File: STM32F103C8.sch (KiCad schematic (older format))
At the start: 25 parts

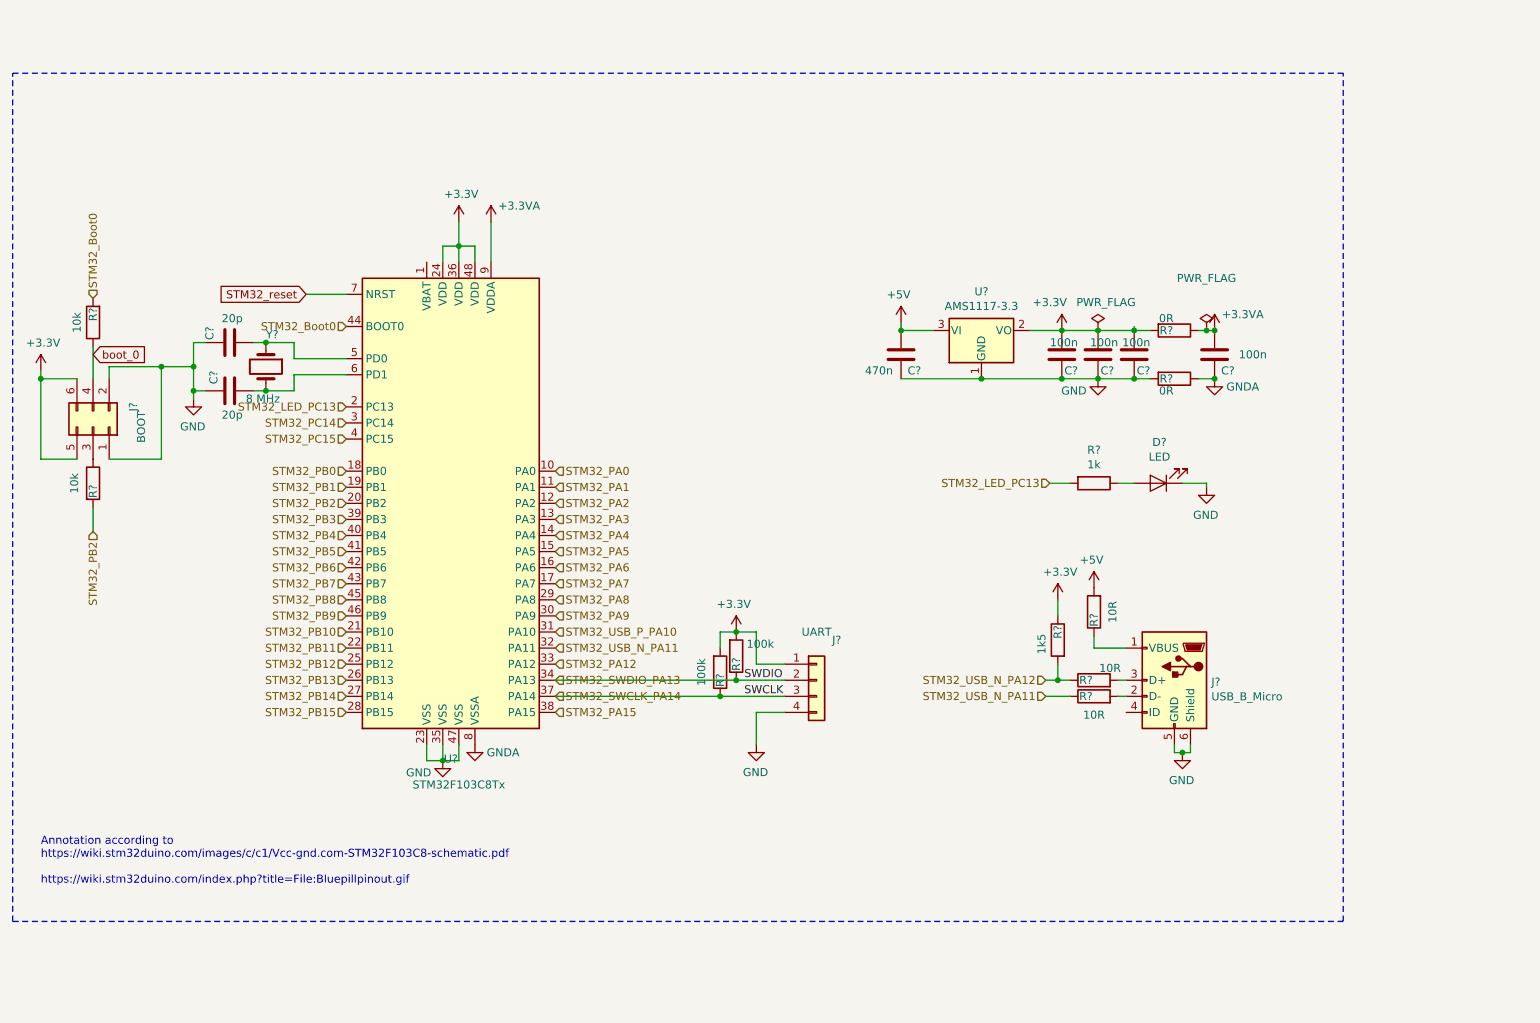
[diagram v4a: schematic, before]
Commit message: Intersheet cleanup
Footprints and cleanup naming on global labels between sheets
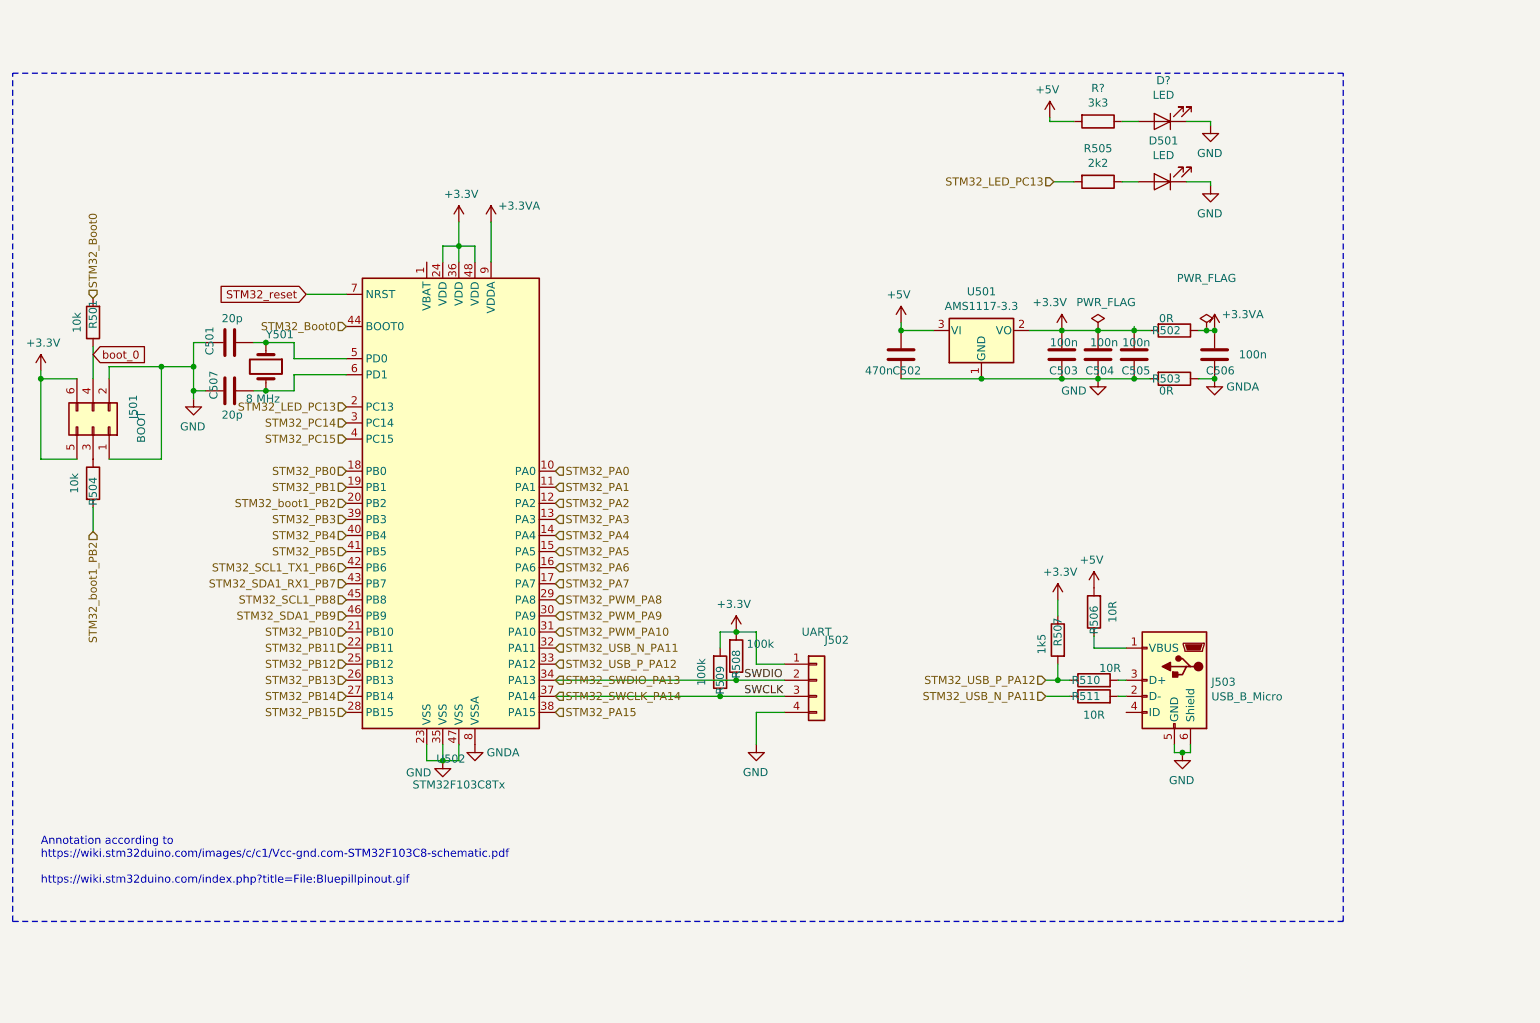
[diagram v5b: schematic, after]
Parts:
- added D?: LED, LED_SMD:LED_0805_2012Metric_Pad1.15x1.40mm_HandSolder, symbol Device:LED
- added R?: 3k3, Resistor_SMD:R_0805_2012Metric_Pad1.15x1.40mm_HandSolder, symbol Device:R
- R505: renamed from R?; value 1k -> 2k2
- gave numbers to parts that had none: 24
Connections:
- net STM32_USB_N_PA12 is gone; now on net STM32_USB_P_PA12: R507.2, R510.1
- net +5V: now also R?.2
- net GND: now also D?.1 (K)
- net STM32_PA12 renamed STM32_USB_P_PA12
- net STM32_PA8 renamed STM32_PWM_PA8
- net STM32_PA9 renamed STM32_PWM_PA9
- net STM32_PB2 renamed STM32_boot1_PB2
- net STM32_PB6 renamed STM32_SCL1_TX1_PB6
- net STM32_PB7 renamed STM32_SDA1_RX1_PB7
- net STM32_PB8 renamed STM32_SCL1_PB8
- net STM32_PB9 renamed STM32_SDA1_PB9
- net STM32_USB_P_PA10 renamed STM32_PWM_PA10
- new net: D?.2 (A), R?.1
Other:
- moved on the sheet: D501, R505

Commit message: LED Matrix ATMega32 rename
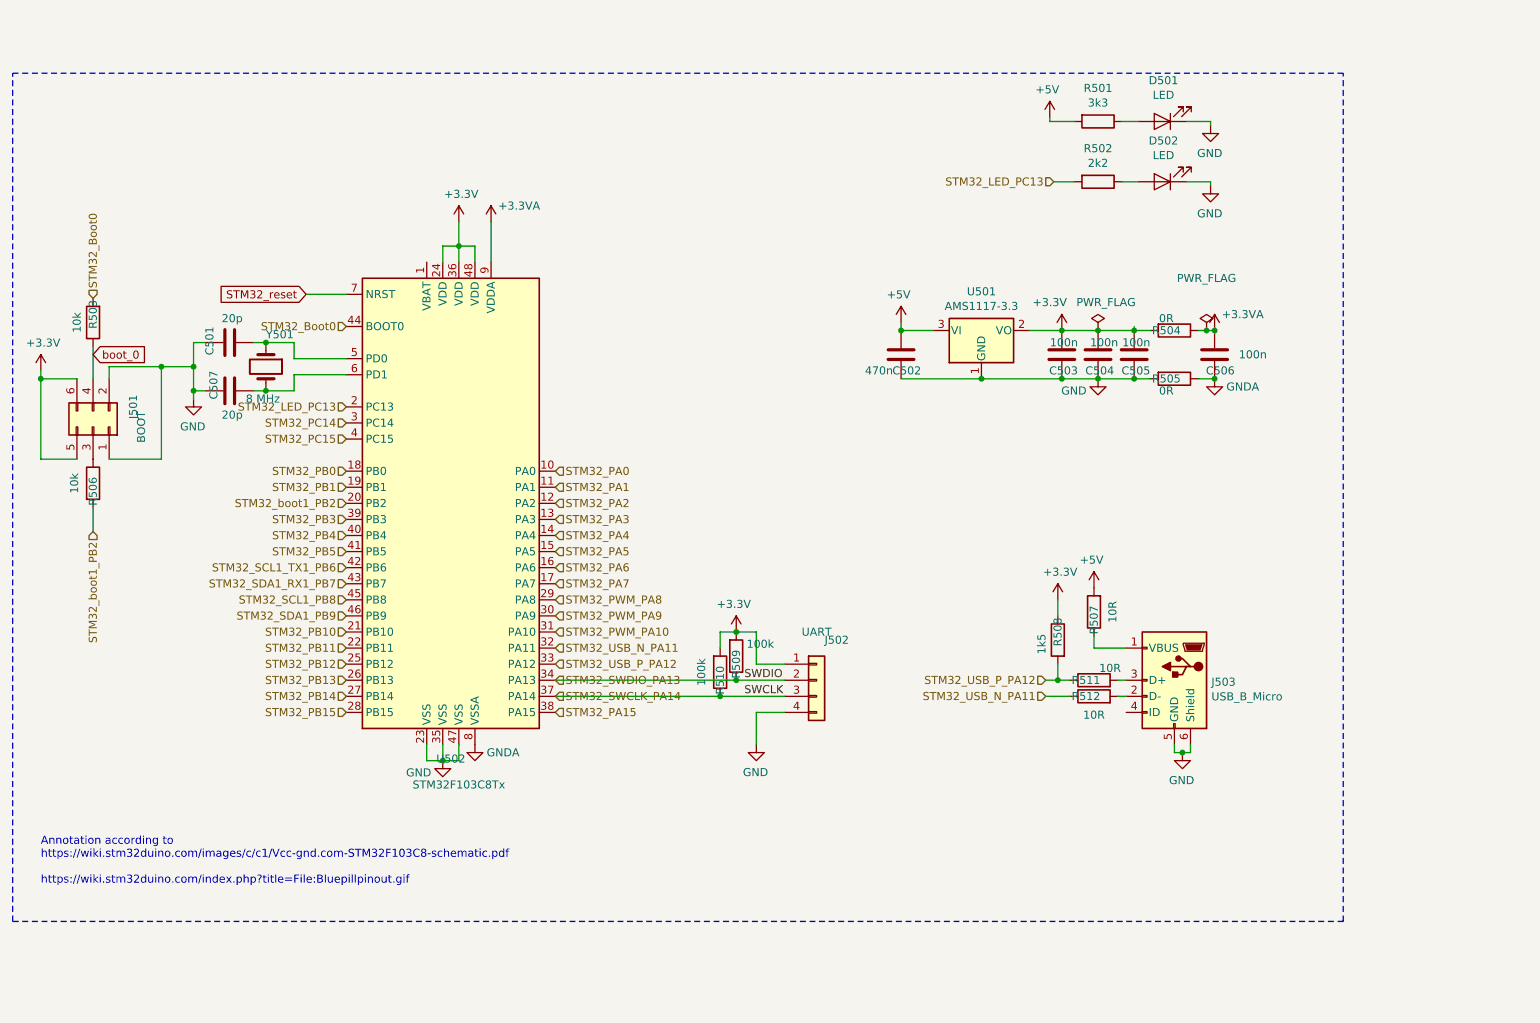
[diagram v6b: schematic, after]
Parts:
- gave numbers to parts that had none: 2
- renumbered D501 to D502, R505 to R502, R501 to R503, R502 to R504, R503 to R505, R504 to R506, R506 to R507, R507 to R508, R508 to R509, R509 to R510, R510 to R511, R511 to R512

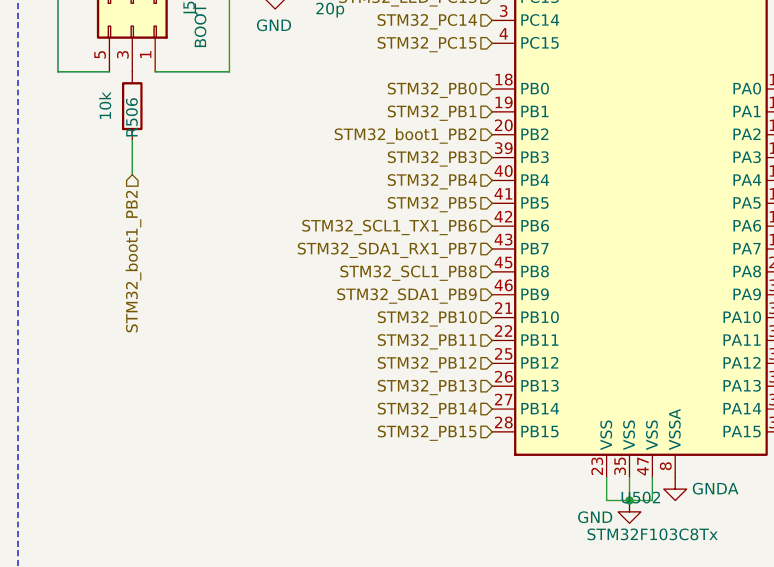
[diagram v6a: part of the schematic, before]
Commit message: STM32 Initiated layout
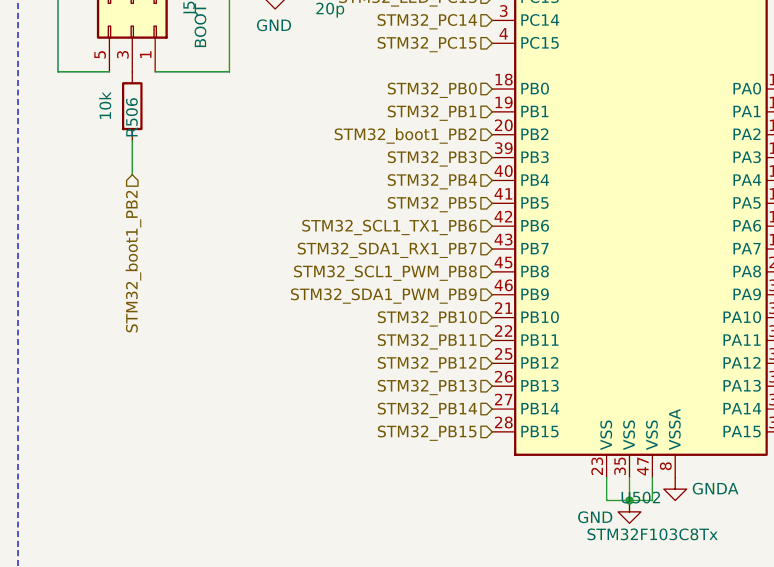
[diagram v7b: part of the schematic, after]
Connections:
- net STM32_SCL1_PB8 renamed STM32_SCL1_PWM_PB8
- net STM32_SDA1_PB9 renamed STM32_SDA1_PWM_PB9
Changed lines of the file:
@@
 STM32_PB10
 Text HLabel 2825 4050 0    50   Input ~ 0
-STM32_SDA1_PB9
+STM32_SDA1_PWM_PB9
 Text HLabel 2825 3950 0    50   Input ~ 0
-STM32_SCL1_PB8
+STM32_SCL1_PWM_PB8
 Text HLabel 2825 3850 0    50   Input ~ 0
 STM32_SDA1_RX1_PB7

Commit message: ERC Performed
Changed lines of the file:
@@
-$Comp
-L power:PWR_FLAG #FLG?
-U 1 1 5CEECE83
-P 7500 2275
-AR Path="/5CE3E7A9/5CD3F059/5CEECE83" Ref="#FLG?"  Part="1"
-AR Path="/5CE53731/5CEC50C7/5CEECE83" Ref="#FLG0501"  Part="1"
-F 0 "#FLG0501" H 7500 2350 50  0001 C CNN
-F 1 "PWR_FLAG" H 7550 2450 50  0000 C CNN
-F 2 "" H 7500 2275 50  0001 C CNN
-F 3 "~" H 7500 2275 50  0001 C CNN
-	1    7500 2275
-	1    0    0    -1
-$EndComp
 $Comp
 L power:PWR_FLAG #FLG?
